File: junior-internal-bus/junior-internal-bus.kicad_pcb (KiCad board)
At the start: 2 copper layers, 99.1 x 45.6 mm, 2 parts, among them J1 C64AC, J2 C64AC

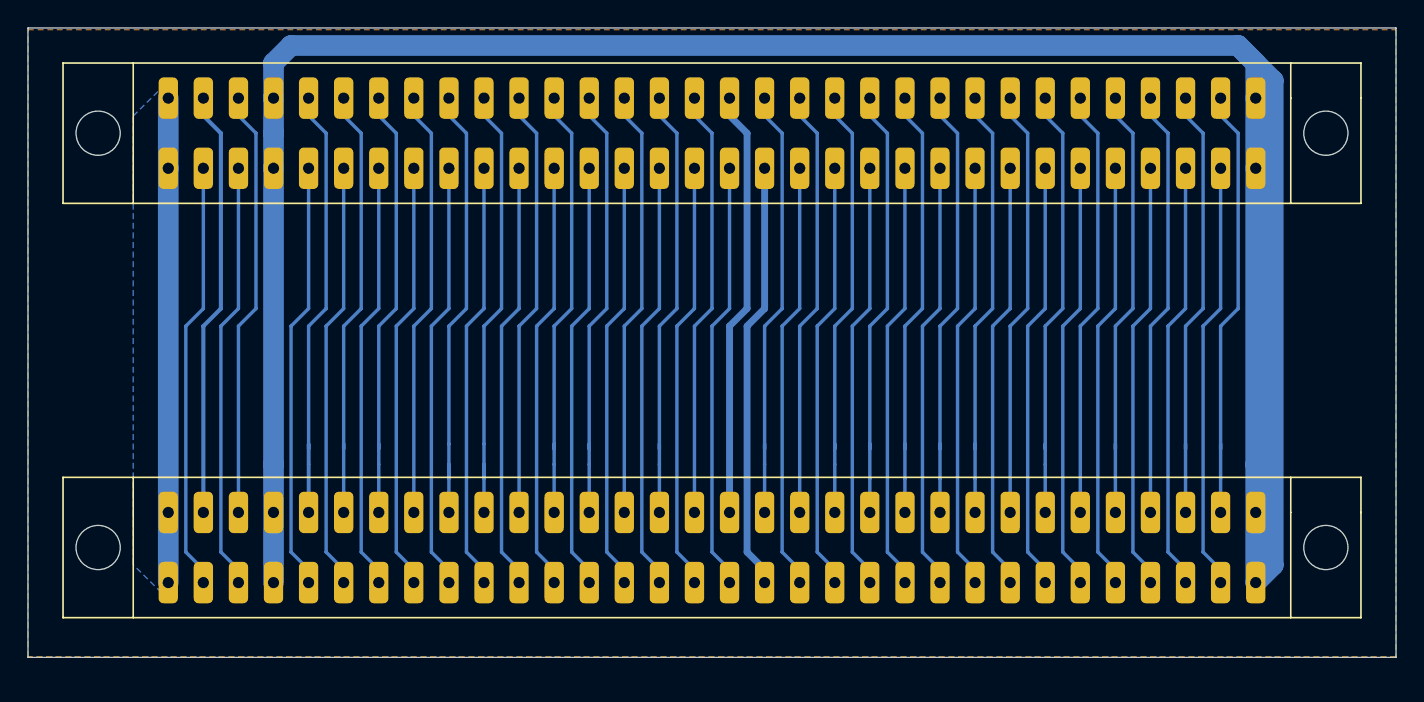
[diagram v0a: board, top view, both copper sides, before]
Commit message: fix - bad DIN41612 footprint, bad distance between connectors
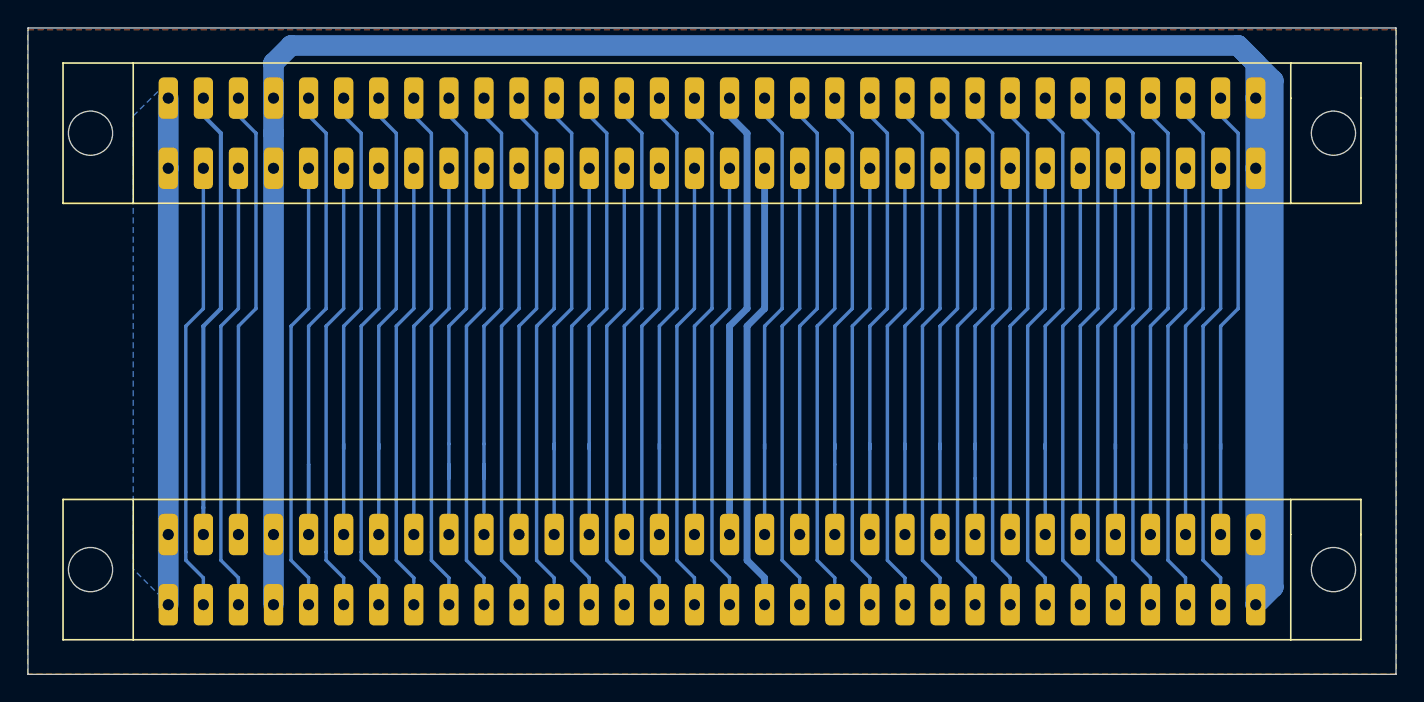
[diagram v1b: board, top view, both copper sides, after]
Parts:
- moved J2 1.60 mm to (91.4, 101.6)
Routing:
- net GND: track 187.9 -> 192.7 mm
- net Net-(J1-3C): track 29.8 -> 32.7 mm
- net Net-(J1-2C): track 31.0 -> 32.7 mm
- net Net-(J1-13C): track 31.4 -> 33.0 mm
- net Net-(J1-6C): track 31.4 -> 33.0 mm
- net Net-(J1-31C): track 31.4 -> 33.0 mm
- net Net-(J1-27C): track 31.1 -> 32.7 mm
- net Net-(J1-16C): track 31.1 -> 32.7 mm
- net /S0: track 31.1 -> 32.7 mm
- net /RW: track 31.1 -> 32.7 mm
- net /K6: track 31.4 -> 33.0 mm
- net /K3: track 31.4 -> 33.0 mm
- net /K2: track 31.4 -> 33.0 mm
- net /D4: track 32.1 -> 33.7 mm
- net /D2: track 31.1 -> 32.7 mm
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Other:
- board size 99.1 x 45.6 mm -> 99.1 x 46.8 mm
